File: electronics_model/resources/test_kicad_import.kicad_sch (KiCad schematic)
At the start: 3 parts

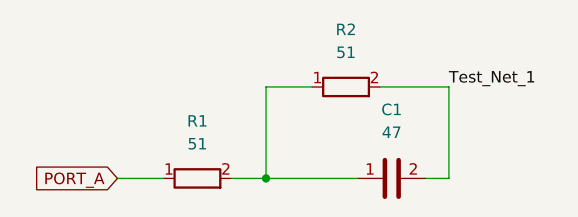
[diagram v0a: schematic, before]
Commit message: kicad import working
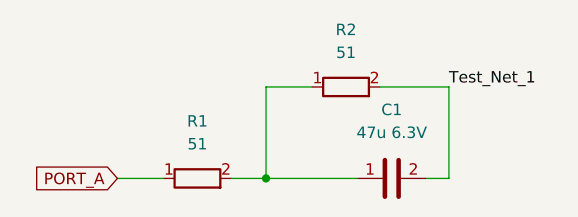
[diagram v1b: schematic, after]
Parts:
- C1: value 47 -> 47u 6.3V
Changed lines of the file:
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@@
     (in_bom yes) (on_board yes) (fields_autoplaced)
     (property "Reference" "C1" (id 0) (at 105.41 88.9 90))
-    (property "Value" "47" (id 1) (at 105.41 91.44 90))
+    (property "Value" "47u 6.3V" (id 1) (at 105.41 91.44 90))
     (property "Footprint" "" (id 2) (at 109.22 95.5548 0)
       (effects (font (size 1.27 1.27)) hide)
@@
   (symbol_instances
     (path "/e8ed392d-e797-4a51-a62e-0d0cb2854712"
-      (reference "C1") (unit 1) (value "47") (footprint "")
+      (reference "C1") (unit 1) (value "47u 6.3V") (footprint "")
     )
     (path "/691e9d02-a5cc-48a1-b9c1-b97da20de9cd"

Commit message: Refactor examples / libraries to use import KiCad schematics (#184)
Refactors a lot of analog blocks (most opamp topologies, analog
switches) to be KiCad importable blocks (by defining a symbol pin
mapping) and/or KiCad imported schematics. Adds custom symbols for many
of these parts, some KiCad's base symbol library for the most part lacks
abstract / generic and high-level parts.

Netlists of example designs should not have changed.

KiCad import behavior change:
- global labels must connect to either a node or external block port and
are not treated as link names
- net labels are used as link names and must not collide with any
existing object member
- add unit tests for the above
- schematic now works on a fixed grid so points can be rounded to the
nearest point that lines up - it turns out points on schematic files can
be off by like 0.05 or something which broke the previous netlister
- support power nets (eg, GND, Vcc symbols)
- power nets and all labels are treated as connected in the schematic
importer (instead of punted up to the block to be handled as connected
in separate connect statements)
- support inline modified symbols (lib_name vs lib_id)
- support symbol mirror, fix rotation calculation (and unit test all of
this)
- import blocks in schematic in xy order (or optionally file order -
this isn't used)
- add a `file_path` utility function to KiCadSchematicBlock which
returns a relative path from the calling file
- moves some tests (mainly rotation, mirror, symbol connectivity) to be
schematic parser tests only, because it's a bit extra (and probably
doesn't tell us much more) to go all the way to Block proto

Infrastructural changes:
- refactors some existing symbol mappings to use pin names instead of
numbers
- refactors some existing symbol mappings to use Mapping return type
which is type covariant
- for connection type errors (link inference errors), prints the names
of the ports involved
- some better error 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
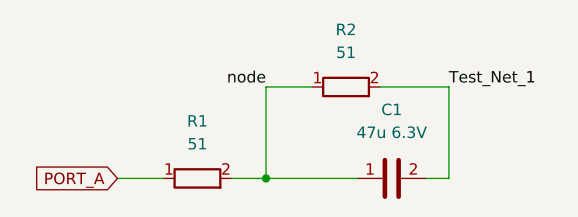
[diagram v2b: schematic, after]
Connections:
- net node: now reaches C1.1, R1.2, R2.1
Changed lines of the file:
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@@
     (stroke (width 0) (type default) (color 0 0 0 0))
+  )
+  (label "node" (at 91.44 86.36 180)
+    (effects (font (size 1.27 1.27)) (justify right bottom))
   )
   (label "Test_Net_1" (at 111.76 86.36 0)
@@
     )
   )
-  (symbol (lib_name "R_1") (lib_id "Device:R") (at 100.33 86.36 90) (unit 1)
-    (in_bom yes) (on_board yes) (fields_autoplaced)
-    (property "Reference" "R2" (id 0) (at 100.33 80.01 90))
-    (property "Value" "51" (id 1) (at 100.33 82.55 90))
-    (property "Footprint" "" (id 2) (at 100.33 88.138 90)
-      (effects (font (size 1.27 1.27)) hide)
-    )
-    (property "Datasheet" "~" (id 3) (at 100.33 86.36 0)
-      (effects (font (size 1.27 1.27)) hide)
-    )
-    (pin "1")
-    (pin "2")
-  )
   (symbol (lib_id "Device:R") (at 83.82 96.52 90) (unit 1)
     (in_bom yes) (on_board yes) (fields_autoplaced)
@@
     )
     (property "Datasheet" "~" (id 3) (at 83.82 96.52 0)
+      (effects (font (size 1.27 1.27)) hide)
+    )
+    (pin "1")
+    (pin "2")
+  )
+  (symbol (lib_id "Device:R") (at 100.33 86.36 90) (unit 1)
+    (in_bom yes) (on_board yes) (fields_autoplaced)
+    (property "Reference" "R2" (id 0) (at 100.33 80.01 90))
+    (property "Value" "51" (id 1) (at 100.33 82.55 90))
+    (property "Footprint" "" (id 2) (at 100.33 88.138 90)
+      (effects (font (size 1.27 1.27)) hide)
+    )
+    (property "Datasheet" "~" (id 3) (at 100.33 86.36 0)
       (effects (font (size 1.27 1.27)) hide)
     )
@@
       (reference "R1") (unit 1) (value "51") (footprint "")
     )
-    (path "/053518b3-994e-4e57-8f86-80f07be5a072"
+    (path "/a8f9f58a-4aa6-48fb-915f-461e000613f8"
       (reference "R2") (unit 1) (value "51") (footprint "")
     )

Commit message: bunch'o'changes
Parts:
- R2: value 51 -> 51 ±5%
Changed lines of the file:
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@@
     (in_bom yes) (on_board yes) (fields_autoplaced)
     (property "Reference" "R2" (id 0) (at 100.33 80.01 90))
-    (property "Value" "51" (id 1) (at 100.33 82.55 90))
+    (property "Value" "51 ±5%" (id 1) (at 100.33 82.55 90))
     (property "Footprint" "" (id 2) (at 100.33 88.138 90)
       (effects (font (size 1.27 1.27)) hide)
@@
     )
     (path "/a8f9f58a-4aa6-48fb-915f-461e000613f8"
-      (reference "R2") (unit 1) (value "51") (footprint "")
+      (reference "R2") (unit 1) (value "51 ±5%") (footprint "")
     )
   )

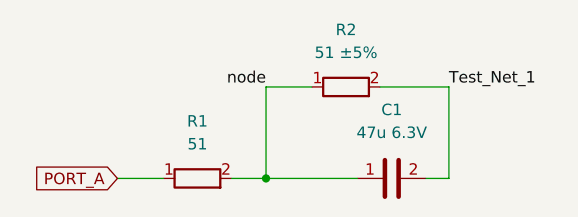
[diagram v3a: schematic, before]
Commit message: unify naming
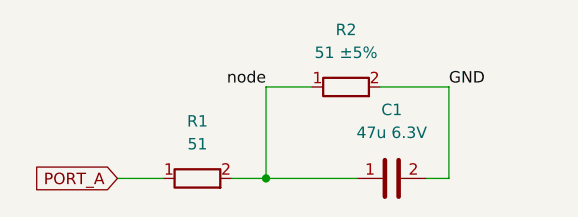
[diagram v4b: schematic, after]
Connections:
- net Test_Net_1 renamed GND
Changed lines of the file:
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@@
     (effects (font (size 1.27 1.27)) (justify right bottom))
   )
-  (label "Test_Net_1" (at 111.76 86.36 0)
+  (label "GND" (at 111.76 86.36 0)
     (effects (font (size 1.27 1.27)) (justify left bottom))
   )
